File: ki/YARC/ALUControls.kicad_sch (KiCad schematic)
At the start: 9 parts, among them U124 74LS08, U126 74LS08, U127 74LS74, U129 74LS574, U130 74LS157, U131 74LS245, U136 74LS32, U137 74HC00, U93 74LS32

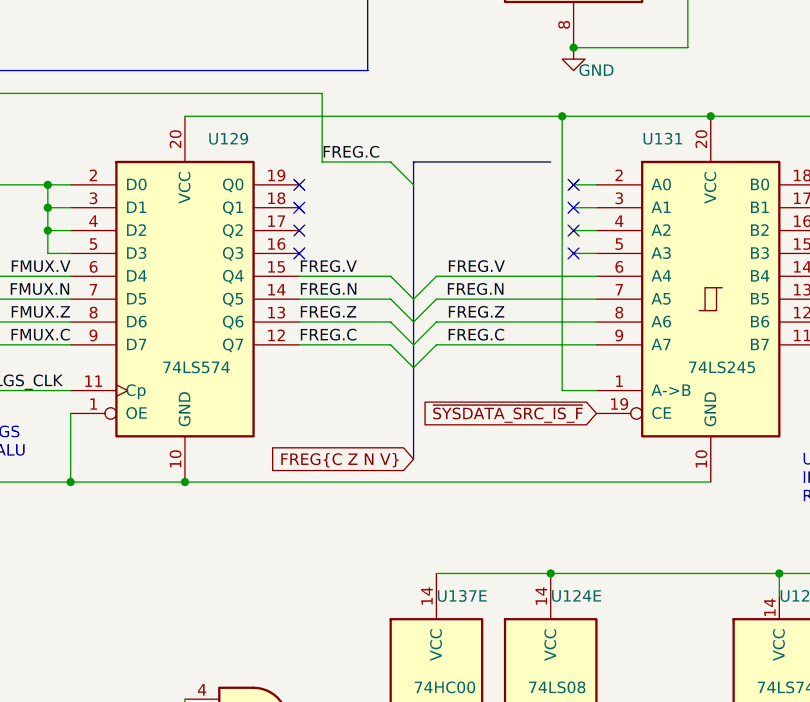
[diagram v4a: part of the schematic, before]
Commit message: Revise SET# logic for LD_UCODE_CTR#. Fix minor errors with no functional consequences (schematic didn't match reality)
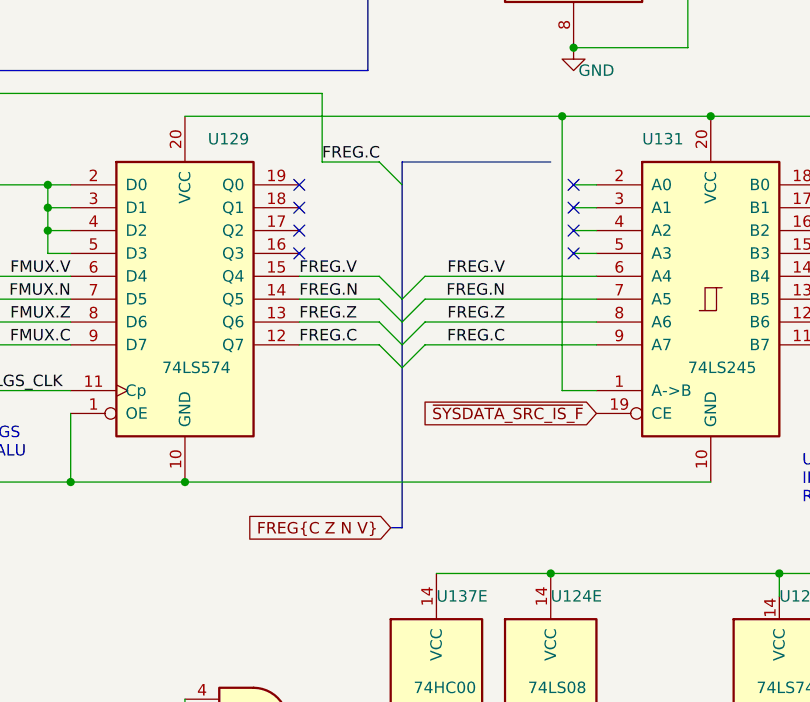
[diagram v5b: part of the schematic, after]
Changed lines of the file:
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@@
     (stroke (width 0) (type default))
   )
-  (bus_entry (at 193.04 114.3) (size 2.54 -2.54)
+  (bus_entry (at 191.77 114.3) (size 2.54 -2.54)
     (stroke (width 0) (type default))
   )
@@
     (stroke (width 0) (type default))
   )
-  (bus_entry (at 193.04 114.3) (size -2.54 -2.54)
+  (bus_entry (at 191.77 114.3) (size -2.54 -2.54)
     (stroke (width 0) (type default))
   )
@@
     (stroke (width 0) (type default))
   )
-  (bus_entry (at 193.04 99.06) (size -2.54 -2.54)
+  (bus_entry (at 191.77 99.06) (size -2.54 -2.54)
     (stroke (width 0) (type default))
   )
@@
     (stroke (width 0) (type default))
   )
-  (bus_entry (at 193.04 119.38) (size -2.54 -2.54)
+  (bus_entry (at 191.77 119.38) (size -2.54 -2.54)
     (stroke (width 0) (type default))
   )
@@
     (stroke (width 0) (type default))
   )
-  (bus_entry (at 193.04 111.76) (size 2.54 -2.54)
+  (bus_entry (at 191.77 111.76) (size 2.54 -2.54)
     (stroke (width 0) (type default))
   )
@@
     (stroke (width 0) (type default))
   )
-  (bus_entry (at 193.04 116.84) (size -2.54 -2.54)
+  (bus_entry (at 191.77 116.84) (size -2.54 -2.54)
     (stroke (width 0) (type default))
   )
@@
     (stroke (width 0) (type default))
   )
-  (bus_entry (at 193.04 119.38) (size 2.54 -2.54)
+  (bus_entry (at 191.77 119.38) (size 2.54 -2.54)
     (stroke (width 0) (type default))
   )
@@
     (stroke (width 0) (type default))
   )
-  (bus_entry (at 193.04 116.84) (size 2.54 -2.54)
-    (stroke (width 0) (type default))
-  )
-  (bus_entry (at 193.04 111.76) (size -2.54 -2.54)
+  (bus_entry (at 191.77 116.84) (size 2.54 -2.54)
+    (stroke (width 0) (type default))
+  )
+  (bus_entry (at 191.77 111.76) (size -2.54 -2.54)
     (stroke (width 0) (type default))
   )
@@
     (stroke (width 0) (type default))
   )
-  (wire (pts (xy 190.5 111.76) (xy 180.34 111.76))
+  (wire (pts (xy 189.23 111.76) (xy 180.34 111.76))
     (stroke (width 0) (type default))
   )
@@
     (stroke (width 0) (type default))
   )
-  (wire (pts (xy 195.58 114.3) (xy 213.36 114.3))
+  (wire (pts (xy 194.31 114.3) (xy 213.36 114.3))
     (stroke (width 0) (type default))
   )
@@
     (stroke (width 0) (type default))
   )
-  (bus (pts (xy 193.04 96.52) (xy 208.28 96.52))
+  (bus (pts (xy 191.77 96.52) (xy 208.28 96.52))
     (stroke (width 0) (type default))
   )
@@
     (stroke (width 0) (type default))
   )
-  (wire (pts (xy 190.5 116.84) (xy 180.34 116.84))
+  (wire (pts (xy 189.23 116.84) (xy 180.34 116.84))
     (stroke (width 0) (type default))
   )
@@
     (stroke (width 0) (type default))
   )
-  (bus (pts (xy 193.04 119.38) (xy 193.04 129.54))
+  (bus (pts (xy 191.77 119.38) (xy 191.77 137.16))
     (stroke (width 0) (type default))
   )
@@
     (stroke (width 0) (type default))
   )
-  (wire (pts (xy 190.5 114.3) (xy 180.34 114.3))
+  (wire (pts (xy 189.23 114.3) (xy 180.34 114.3))
     (stroke (width 0) (type default))
   )
@@
     (stroke (width 0) (type default))
   )
-  (wire (pts (xy 195.58 116.84) (xy 213.36 116.84))
-    (stroke (width 0) (type default))
-  )
-  (bus (pts (xy 193.04 99.06) (xy 193.04 111.76))
-    (stroke (width 0) (type default))
-  )
-  (wire (pts (xy 195.58 109.22) (xy 213.36 109.22))
+  (wire (pts (xy 194.31 116.84) (xy 213.36 116.84))
+    (stroke (width 0) (type default))
+  )
+  (bus (pts (xy 191.77 99.06) (xy 191.77 111.76))
+    (stroke (width 0) (type default))
+  )
+  (wire (pts (xy 194.31 109.22) (xy 213.36 109.22))
     (stroke (width 0) (type default))
   )
@@
     (stroke (width 0) (type default))
   )
-  (bus (pts (xy 193.04 116.84) (xy 193.04 119.38))
+  (bus (pts (xy 191.77 116.84) (xy 191.77 119.38))
     (stroke (width 0) (type default))
   )
@@
     (stroke (width 0) (type default))
   )
-  (bus (pts (xy 193.04 96.52) (xy 193.04 99.06))
+  (bus (pts (xy 191.77 96.52) (xy 191.77 99.06))
     (stroke (width 0) (type default))
   )
@@
     (stroke (width 0) (type default))
   )
-  (bus (pts (xy 193.04 111.76) (xy 193.04 114.3))
+  (bus (pts (xy 191.77 111.76) (xy 191.77 114.3))
     (stroke (width 0) (type default))
   )
@@
     (stroke (width 0) (type default))
   )
-  (wire (pts (xy 195.58 111.76) (xy 213.36 111.76))
+  (wire (pts (xy 194.31 111.76) (xy 213.36 111.76))
     (stroke (width 0) (type default))
   )
@@
     (stroke (width 0) (type default))
   )
-  (wire (pts (xy 190.5 109.22) (xy 180.34 109.22))
+  (wire (pts (xy 189.23 109.22) (xy 180.34 109.22))
     (stroke (width 0) (type default))
   )
@@
     (stroke (width 0) (type default))
   )
-  (bus (pts (xy 193.04 114.3) (xy 193.04 116.84))
+  (bus (pts (xy 191.77 114.3) (xy 191.77 116.84))
     (stroke (width 0) (type default))
   )
@@
     (stroke (width 0) (type default))
   )
-  (wire (pts (xy 190.5 96.52) (xy 182.88 96.52))
+  (wire (pts (xy 189.23 96.52) (xy 182.88 96.52))
     (stroke (width 0) (type default))
   )
@@
   )
   (wire (pts (xy 129.54 187.96) (xy 129.54 193.04))
+    (stroke (width 0) (type default))
+  )
+  (bus (pts (xy 190.5 137.16) (xy 191.77 137.16))
     (stroke (width 0) (type default))
   )
@@
     )
   )
+  (global_label "FREG{C Z N V}" (shape input) (at 190.5 137.16 180) (fields_autoplaced)
+    (effects (font (size 1.27 1.27)) (justify right))
+    (property "Intersheetrefs" "${INTERSHEET_REFS}" (at 173.2424 137.16 0)
+      (effects (font (size 1.27 1.27)) (justify right) hide)
+    )
+  )
   (global_label "SYSCLK" (shape input) (at 25.4 153.67 180) (fields_autoplaced)
     (effects (font (size 1.27 1.27)) (justify right))
@@
     )
   )
-  (global_label "FREG{C Z N V}" (shape input) (at 193.04 129.54 180) (fields_autoplaced)
-    (effects (font (size 1.27 1.27)) (justify right))
-    (property "Intersheetrefs" "${INTERSHEET_REFS}" (at 175.7824 129.54 0)
-      (effects (font (size 1.27 1.27)) (justify right) hide)
-    )
-  )
   (global_label "FQTR{C Z N V}" (shape input) (at 30.48 17.78 180) (fields_autoplaced)
     (effects (font (size 1.27 1.27)) (justify right))
@@
     )
   )
+  (global_label "~{SYSDATA_SRC_IS_F}" (shape input) (at 213.36 124.46 180) (fields_autoplaced)
+    (effects (font (size 1.27 1.27)) (justify right))
+    (property "Intersheetrefs" "${INTERSHEET_REFS}" (at 193.4693 124.5394 0)
+      (effects (font (size 1.27 1.27)) (justify right) hide)
+    )
+  )
   (global_label "K[0..31]" (shape input) (at 15.24 127 270) (fields_autoplaced)
     (effects (font (size 1.27 1.27)) (justify right))
@@
       (effects (font (size 1.27 1.27)) (justify right) hide)
     )
-  )
-  (global_label "~{SYSDATA_SRC_IS_F}" (shape input) (at 213.36 124.46 180) (fields_autoplaced)
-    (effects (font (size 1.27 1.27)) (justify right))
-    (property "Intersheetrefs" "${INTERSHEET_REFS}" (at 193.4693 124.5394 0)
-      (effects (font (size 1.27 1.27)) (justify right) hide)
-    )
